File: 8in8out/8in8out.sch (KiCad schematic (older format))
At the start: 119 parts, among them IC1 ATTINY2313-P, K110 G5T-1-12VDC, K120 G5T-1-12VDC, K130 G5T-1-12VDC, K140 G5T-1-12VDC, K150 G5T-1-12VDC, K160 G5T-1-12VDC, K170 G5T-1-12VDC, K180 G5T-1-12VDC, P100 CONN_2, P101 CONN_2, P102 CONN_2, P103 CONN_2, P110 CONN_2, P111 CONN_2, P12 CONN_2, P120 CONN_2, P120 CONN_6, P121 CONN_6, P130 CONN_2, P130 CONN_3X2, P140 CONN_2, P150 CONN_2, P160 CONN_2, P170 CONN_2, P180 CONN_2, P34 CONN_2, P56 CONN_2, P78 CONN_2, Q110 NPN, Q120 NPN, Q130 NPN, Q140 NPN, Q150 NPN, Q160 NPN, Q170 NPN, Q180 NPN, U10 OPTO-TRANSISTOR, U20 OPTO-TRANSISTOR, U30 OPTO-TRANSISTOR, U40 OPTO-TRANSISTOR, U50 OPTO-TRANSISTOR, U60 OPTO-TRANSISTOR, U70 OPTO-TRANSISTOR, U80 OPTO-TRANSISTOR

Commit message: Mise ? jour Draft
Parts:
- removed P12, P34, P56, P78: CONN_2, symbol CONN_2
- removed R12, R22, R32, R42, R52, R62, R72, R82: R, symbol R
- added J1, J2: RJ45, symbol RJ45
- added P?: CONN_9, symbol CONN_9
- added U?: 74HC595, symbol 74HC595
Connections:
- net labels added: IN4, IN5, IN6, IN7, INO, SCL, SCL(GND), SDA, SDA(GND)
- wire segments 243 -> 227

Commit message: Ajout 74HC165 sur les entr?es + pull up Creation du connecteur mini 5 poles Debut routage
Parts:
- removed P121: CONN_6, symbol CONN_6
- removed P?: CONN_9, symbol CONN_9
- added P1, P2: CONN_5, symbol CONN_5
- added P107: CONN_3, symbol CONN_3
- added P109: CONN_2, symbol CONN_2
- added R12, R22, R32, R42, R52, R62, R72, R82: R, symbol R
- added U2: 74LS165, symbol 74LS165
- gave numbers to parts that had none: 1
- renumbered P130 to ISP0, P120 to J3, P110 to P105, P111 to P106, R140 to R141, R160 to R161
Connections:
- net labels added: CLK, CLK_IN, CLK_OUT, CMND0, CMND1, CMND2, CMND3, CMND4, CMND5, CMND6, CMND7, DATA, DATA_IN, DATA_OUT, LATCH, LATCH_IN, LATCH_OUT, RX, TX
- net labels removed: INO, SCL, SCL(GND), SDA, SDA(GND)
- wire segments 227 -> 309
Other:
- moved on the sheet: C1, C2, D1, D10, D110, D111, D120, D121, D130, D131, D140, D141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

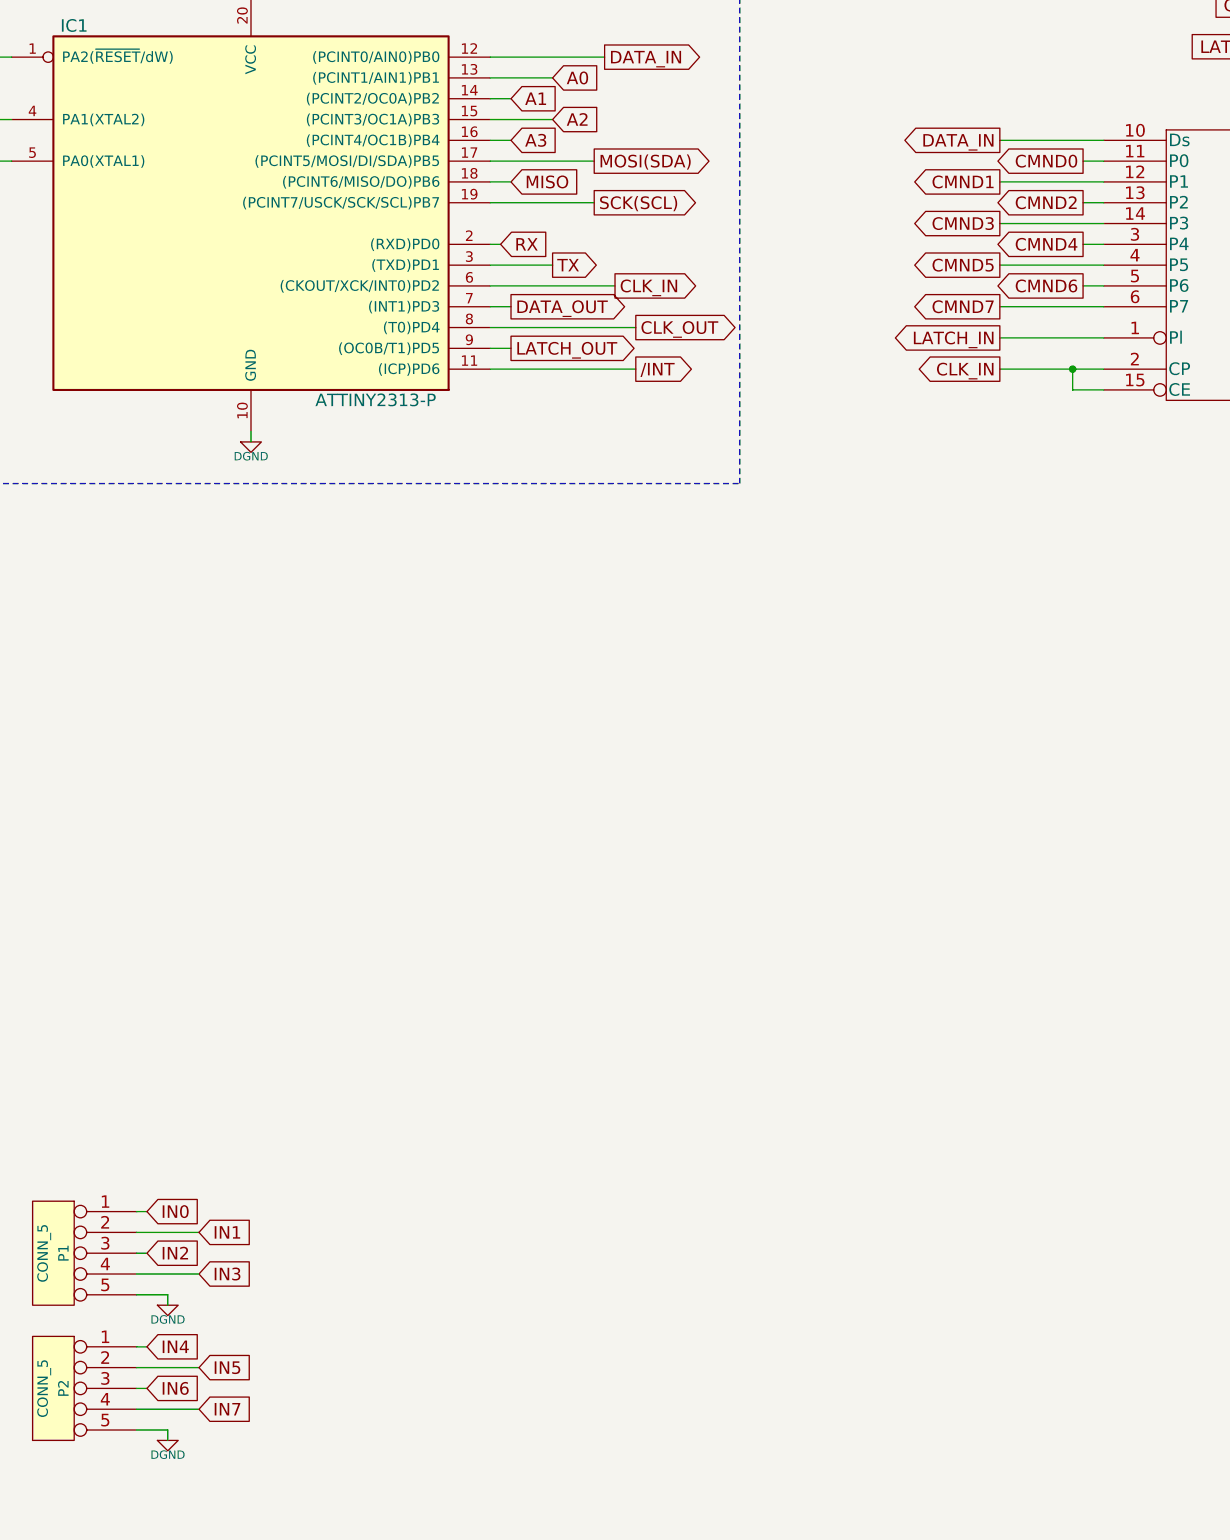
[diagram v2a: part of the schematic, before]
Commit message: Redimensionnement PCB en 100*86
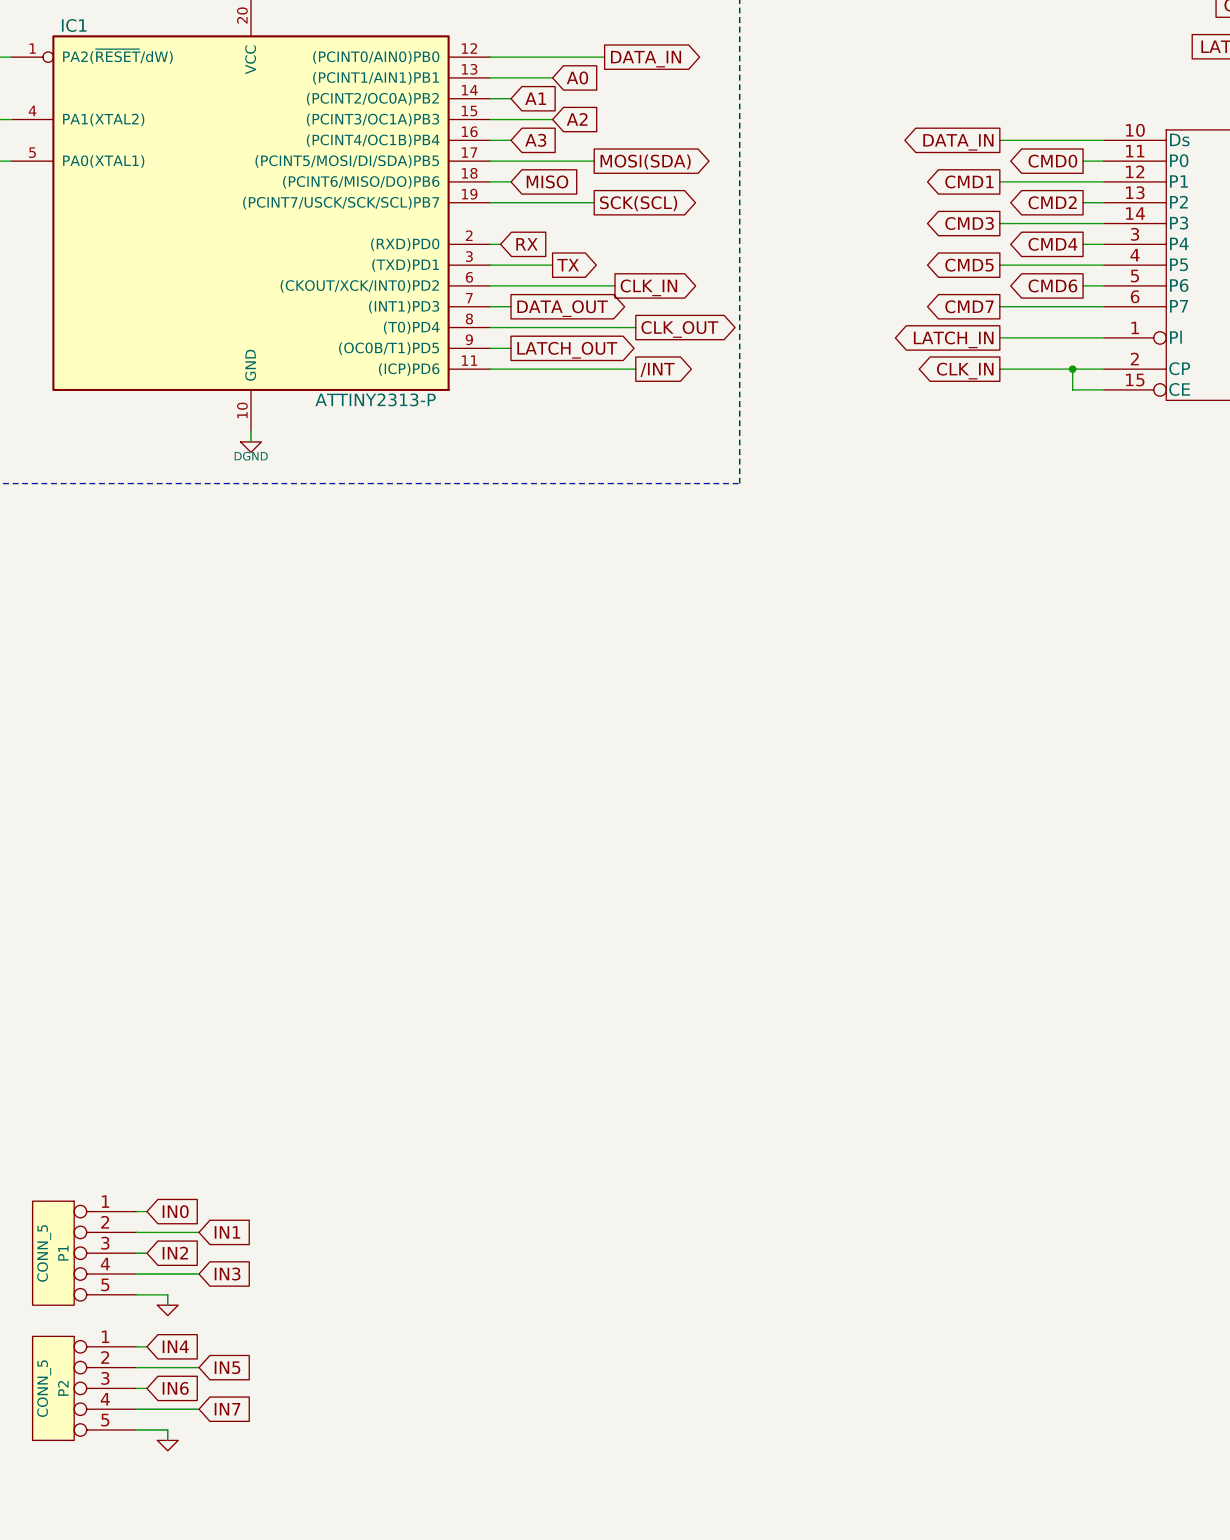
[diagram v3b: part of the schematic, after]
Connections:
- net labels removed: CMND0, CMND1, CMND2, CMND3, CMND4, CMND5, CMND6, CMND7
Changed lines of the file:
@@
-EESchema Schematic File Version 2  date sam. 09 févr. 2013 21:24:44 CET
+EESchema Schematic File Version 2  date dim. 10 févr. 2013 10:46:28 CET
 LIBS:g5la-1-12vdc
 LIBS:power
@@
 Sheet 1 1
 Title "8in 8relays I2C board"
-Date "9 feb 2013"
+Date "10 feb 2013"
 Rev "V0.0"
 Comp "XPLDUINO project"
@@
 CMD7
 Text GLabel 11200 8000 0    60   Output ~ 0
-CMND2
+CMD2
 Text GLabel 11200 7800 0    60   Output ~ 0
-CMND0
+CMD0
 Text GLabel 10800 8100 0    60   Output ~ 0
-CMND3
+CMD3
 Text GLabel 10800 7900 0    60   Output ~ 0
-CMND1
+CMD1
 Text GLabel 11200 8200 0    60   Output ~ 0
-CMND4
+CMD4
 Text GLabel 8850 7800 2    60   Output ~ 0
 MOSI(SDA)
@@
 	5550 5800 5550 3500
 Text GLabel 10800 8500 0    60   Output ~ 0
-CMND7
+CMD7
 Text GLabel 11200 8400 0    60   Output ~ 0
-CMND6
+CMD6
 Text GLabel 10800 8300 0    60   Output ~ 0
-CMND5
+CMD5
 Wire Notes Line
 	9550 6000 9550 9350
@@
 Wire Wire Line
 	6800 13250 6800 13300
-$Comp
-L DGND #PWR091
-U 1 1 5117122F
-P 6800 13300
-F 0 "#PWR091" H 6800 13300 40  0001 C CNN
-F 1 "DGND" H 6800 13230 40  0000 C CNN
-	1    6800 13300
-	1    0    0    -1
-$EndComp
 Wire Wire Line
 	6650 12850 6700 12850
@@
 Wire Wire Line
 	6800 13900 6800 13950
-$Comp
-L DGND #PWR092
-U 1 1 511717B2
-P 6800 13950
-F 0 "#PWR092" H 6800 13950 40  0001 C CNN
-F 1 "DGND" H 6800 13880 40  0000 C CNN
-	1    6800 13950
-	1    0    0    -1
-$EndComp
 Wire Wire Line
 	6650 13500 6700 13500
@@
 Wire Notes Line
 	5250 9350 5550 9350
+$Comp
+L GND #PWR?
+U 1 1 51176AB9
+P 6800 13300
+F 0 "#PWR?" H 6800 13300 30  0001 C CNN
+F 1 "GND" H 6800 13230 30  0001 C CNN
+	1    6800 13300
+	1    0    0    -1
+$EndComp
+$Comp
+L GND #PWR?
+U 1 1 51176ACB
+P 6800 13950
+F 0 "#PWR?" H 6800 13950 30  0001 C CNN
+F 1 "GND" H 6800 13880 30  0001 C CNN
+	1    6800 13950
+	1    0    0    -1
+$EndComp
 $EndSCHEMATC

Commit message: Correction pin data du 74HC165 Ajustement position des composants
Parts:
- P107: symbol CONN_3 -> CONN_5
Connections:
- wire segments 309 -> 314
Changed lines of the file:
@@
-EESchema Schematic File Version 2  date dim. 10 févr. 2013 10:46:28 CET
+EESchema Schematic File Version 2  date dim. 10 févr. 2013 15:59:09 CET
 LIBS:g5la-1-12vdc
 LIBS:power
@@
 Wire Wire Line
 	11300 8650 10800 8650
-Wire Wire Line
-	10800 7700 11300 7700
 Text GLabel 9050 3100 3    60   Output ~ 0
 A0
@@
 Wire Wire Line
 	11150 8900 11300 8900
-Text GLabel 10800 7700 0    60   Output ~ 0
+Text GLabel 12800 7800 2    60   Output ~ 0
 DATA_IN
 Wire Wire Line
@@
 Connection ~ 3800 4500
 Wire Wire Line
-	12250 6750 12250 6950
+	12250 6750 12250 7050
 $Comp
-L CONN_3 P107
+L CONN_5 P107
 U 1 1 51172A2D
-P 12600 7050
-F 0 "P107" V 12550 7050 50  0000 C CNN
-F 1 "CONN_3" V 12650 7050 40  0000 C CNN
-	1    12600 7050
+P 12650 7250
+F 0 "P107" V 12600 7250 50  0000 C CNN
+F 1 "CONN_3" V 12700 7250 40  0000 C CNN
+	1    12650 7250
 	1    0    0    -1
 $EndComp
 Text GLabel 12100 7050 0    60   Input ~ 0
 CLK
-Text GLabel 12100 7250 0    60   Input ~ 0
+Text GLabel 12100 7200 0    60   Input ~ 0
 LATCH
-Wire Wire Line
-	12100 7050 12250 7050
-Wire Wire Line
-	12100 7250 12200 7250
-Wire Wire Line
-	12200 7250 12200 7150
-Wire Wire Line
-	12200 7150 12250 7150
 $Comp
 L CONN_2 P109
@@
 	1    0    0    -1
 $EndComp
+Wire Wire Line
+	12700 7800 12800 7800
+Wire Wire Line
+	12100 7050 12200 7050
+Wire Wire Line
+	12200 7050 12200 7150
+Wire Wire Line
+	12200 7150 12250 7150
+Wire Wire Line
+	12100 7200 12150 7200
+Wire Wire Line
+	12150 7200 12150 7250
+Wire Wire Line
+	12150 7250 12250 7250
+Wire Wire Line
+	12250 7350 12150 7350
+Wire Wire Line
+	12250 7450 12150 7450
+Wire Wire Line
+	12150 7450 12150 7500
+$Comp
+L DGND #PWR?
+U 1 1 5117C4D5
+P 12150 7500
+F 0 "#PWR?" H 12150 7500 40  0001 C CNN
+F 1 "DGND" H 12150 7430 40  0000 C CNN
+	1    12150 7500
+	1    0    0    -1
+$EndComp
+$Comp
+L +5V #PWR?
+U 1 1 5117C4DB
+P 12150 7350
+F 0 "#PWR?" H 12150 7440 20  0001 C CNN
+F 1 "+5V" H 12150 7440 30  0000 C CNN
+	1    12150 7350
+	0    -1   -1   0
+$EndComp
 $EndSCHEMATC
